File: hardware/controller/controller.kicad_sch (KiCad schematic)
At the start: 0 parts

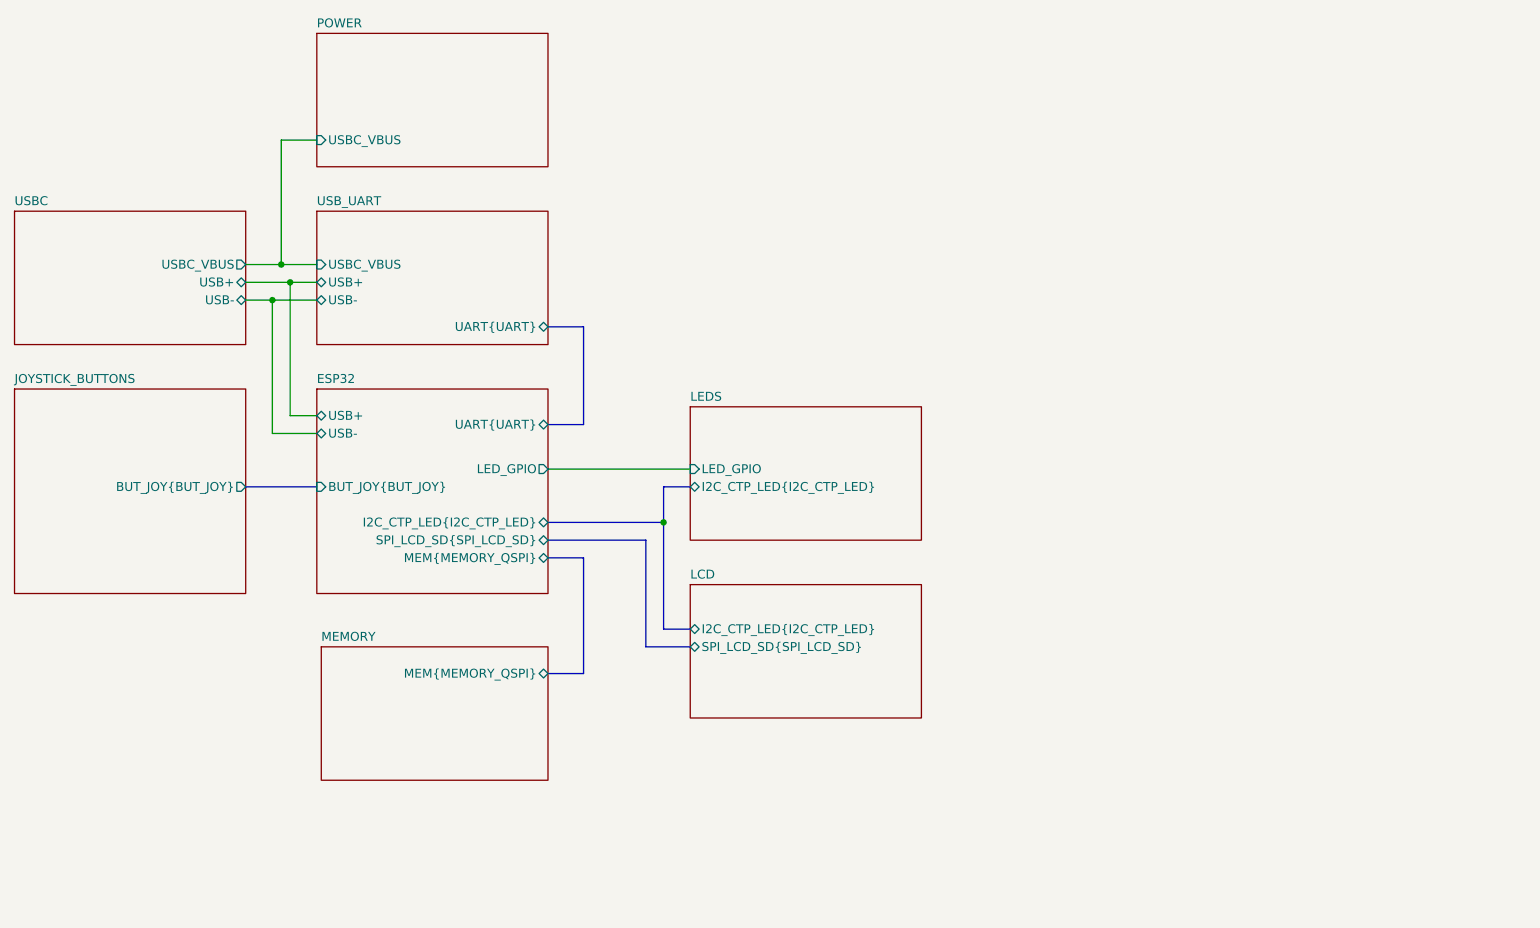
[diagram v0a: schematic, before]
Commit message: Moved LEDs around. Replaced some discrete resistors with resistor arrays. Added mounting holes. Added. Added a lot of actual components for passive elements
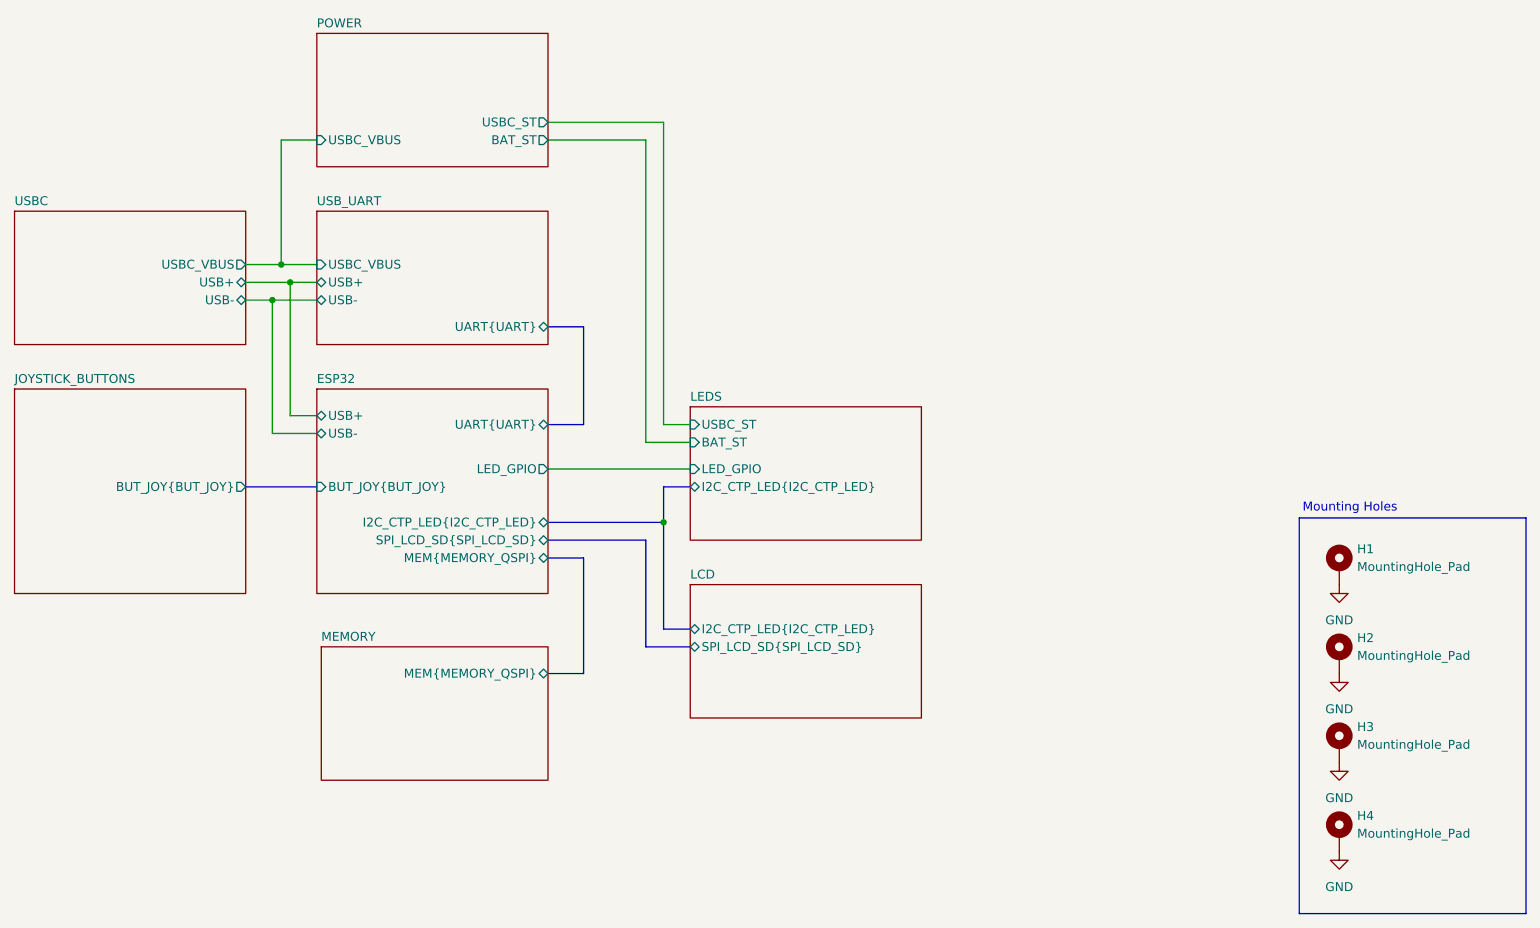
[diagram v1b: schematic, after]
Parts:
- added H1, H2, H3, H4: MountingHole_Pad, SamacSys_Parts:MountingHole_4.3mm_M4_ISO14580_Pad, symbol Mechanical:MountingHole_Pad
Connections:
- new net GND: H1.1, H2.1, H3.1, H4.1
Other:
- sheet LEDS ports: added BAT_ST, USBC_ST; removed none
- sheet POWER ports: added BAT_ST, USBC_ST; removed none
- note added: "Mounting Holes"
- title: Controller -> Remote Controller

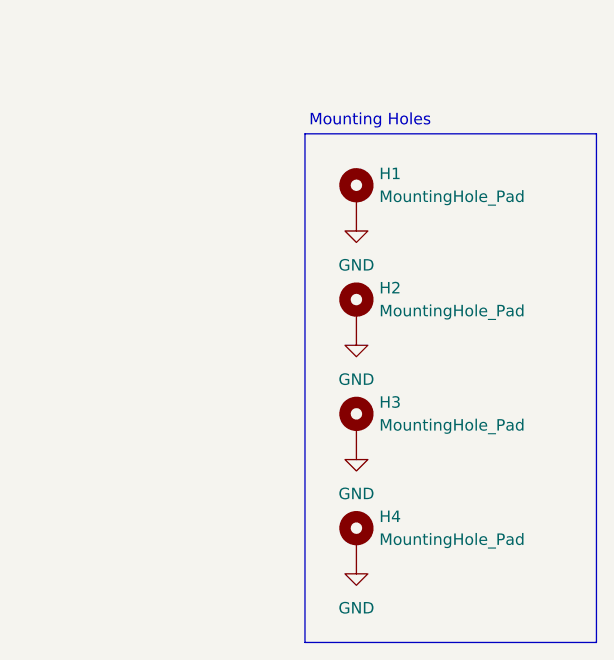
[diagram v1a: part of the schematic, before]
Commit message: ERC good to go. grouped all components on pcb
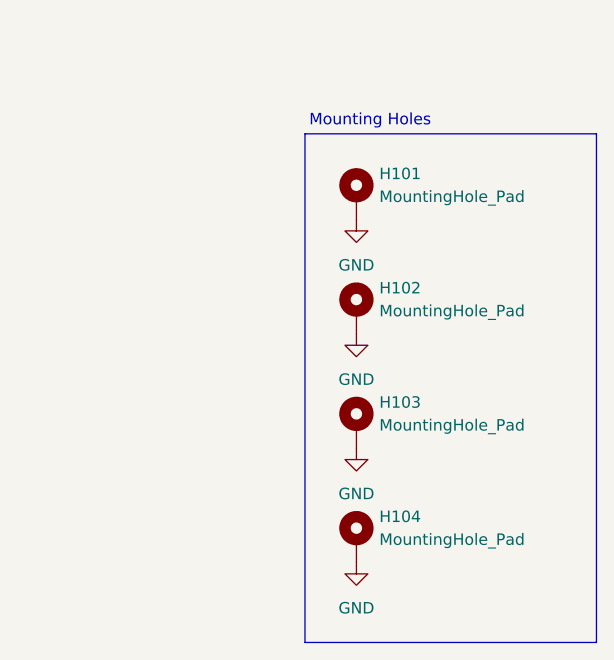
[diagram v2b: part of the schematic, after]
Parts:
- renumbered H1 to H101, H2 to H102, H3 to H103, H4 to H104
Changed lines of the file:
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@@
 		(dnp no)
 		(fields_autoplaced yes)
-		(property "Reference" "#PWR083"
+		(property "Reference" "#PWR0104"
 			(at 247.65 158.75 0)
 			(effects
@@
 			(project "controller"
 				(path "/869bea87-c885-4ead-826b-3f34ceacafad"
-					(reference "#PWR083")
+					(reference "#PWR0104")
 					(unit 1)
 				)
@@
 		(dnp no)
 		(fields_autoplaced yes)
-		(property "Reference" "H3"
+		(property "Reference" "H103"
 			(at 250.19 134.6199 0)
 			(effects
@@
 			(project "controller"
 				(path "/869bea87-c885-4ead-826b-3f34ceacafad"
-					(reference "H3")
+					(reference "H103")
 					(unit 1)
 				)
@@
 		(dnp no)
 		(fields_autoplaced yes)
-		(property "Reference" "#PWR082"
+		(property "Reference" "#PWR0103"
 			(at 247.65 146.05 0)
 			(effects
@@
 			(project "controller"
 				(path "/869bea87-c885-4ead-826b-3f34ceacafad"
-					(reference "#PWR082")
+					(reference "#PWR0103")
 					(unit 1)
 				)
@@
 		(dnp no)
 		(fields_autoplaced yes)
-		(property "Reference" "#PWR079"
+		(property "Reference" "#PWR0102"
 			(at 247.65 133.35 0)
 			(effects
@@
 			(project "controller"
 				(path "/869bea87-c885-4ead-826b-3f34ceacafad"
-					(reference "#PWR079")
+					(reference "#PWR0102")
 					(unit 1)
 				)
@@
 		(dnp no)
 		(fields_autoplaced yes)
-		(property "Reference" "#PWR021"
+		(property "Reference" "#PWR0101"
 			(at 247.65 120.65 0)
 			(effects
@@
 			(project ""
 				(path "/869bea87-c885-4ead-826b-3f34ceacafad"
-					(reference "#PWR021")
+					(reference "#PWR0101")
 					(unit 1)
 				)
@@
 		(dnp no)
 		(fields_autoplaced yes)
-		(property "Reference" "H4"
+		(property "Reference" "H104"
 			(at 250.19 147.3199 0)
 			(effects
@@
 			(project "controller"
 				(path "/869bea87-c885-4ead-826b-3f34ceacafad"
-					(reference "H4")
+					(reference "H104")
 					(unit 1)
 				)
@@
 		(dnp no)
 		(fields_autoplaced yes)
-		(property "Reference" "H1"
+		(property "Reference" "H101"
 			(at 250.19 109.2199 0)
 			(effects
@@
 			(project ""
 				(path "/869bea87-c885-4ead-826b-3f34ceacafad"
-					(reference "H1")
+					(reference "H101")
 					(unit 1)
 				)
@@
 		(dnp no)
 		(fields_autoplaced yes)
-		(property "Reference" "H2"
+		(property "Reference" "H102"
 			(at 250.19 121.9199 0)
 			(effects
@@
 			(project "controller"
 				(path "/869bea87-c885-4ead-826b-3f34ceacafad"
-					(reference "H2")
-					(unit 1)
-				)
+					(reference "H102")
+					(unit 1)
+				)

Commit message: a
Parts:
- added H105: MountingHole, MountingHole:MountingHole_2.2mm_M2_DIN965, symbol Mechanical:MountingHole
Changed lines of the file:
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@@
 	(text "Mounting Holes"
 		(exclude_from_sim no)
-		(at 249.174 103.378 0)
+		(at 248.412 86.614 0)
 		(effects
 			(font
@@
 	(text_box "\n"
 		(exclude_from_sim no)
-		(at 241.935 104.775 0)
-		(size 32.385 56.515)
+		(at 241.935 92.075 0)
+		(size 32.385 69.215)
 		(margins 0.9525 0.9525 0.9525 0.9525)
 		(stroke
@@
 	)
 	(symbol
+		(lib_id "Mechanical:MountingHole")
+		(at 247.65 100.33 0)
+		(unit 1)
+		(exclude_from_sim no)
+		(in_bom no)
+		(on_board yes)
+		(dnp no)
+		(fields_autoplaced yes)
+		(property "Reference" "H105"
+			(at 250.19 99.0599 0)
+			(effects
+				(font
+					(size 1.27 1.27)
+				)
+				(justify left)
+			)
+		)
+		(property "Value" "MountingHole"
+			(at 250.19 101.5999 0)
+			(effects
+				(font
+					(size 1.27 1.27)
+				)
+				(justify left)
+			)
+		)
+		(property "Footprint" "MountingHole:MountingHole_2.2mm_M2_DIN965"
+			(at 247.65 100.33 0)
+			(effects
+				(font
+					(size 1.27 1.27)
+				)
+				(hide yes)
+			)
+		)
+		(property "Datasheet" "~"
+			(at 247.65 100.33 0)
+			(effects
+				(font
+					(size 1.27 1.27)
+				)
+				(hide yes)
+			)
+		)
+		(property "Description" "Mounting Hole without connection"
+			(at 247.65 100.33 0)
+			(effects
+				(font
+					(size 1.27 1.27)
+				)
+				(hide yes)
+			)
+		)
+		(instances
+			(project ""
+				(path "/869bea87-c885-4ead-826b-3f34ceacafad"
+					(reference "H105")
+					(unit 1)
+				)
+			)
+		)
+	)
+	(symbol
 		(lib_id "Mechanical:MountingHole_Pad")
 		(at 247.65 124.46 0)
@@
 		(size 33.02 19.05)
 		(exclude_from_sim no)
-		(in_bom yes)
-		(on_board yes)
-		(dnp no)
-		(fields_autoplaced yes)
-		(stroke
+		(in_bom no)
+		(on_board no)
+		(dnp yes)
+		(fields_autoplaced yes)
+		(stroke

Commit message: save before nuke
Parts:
- renumbered H105 to H101, H101 to H102, H102 to H103, H103 to H104, H104 to H105
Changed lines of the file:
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@@
 		(dnp no)
 		(fields_autoplaced yes)
-		(property "Reference" "H103"
+		(property "Reference" "H104"
 			(at 250.19 134.6199 0)
 			(effects
@@
 			(project "controller"
 				(path "/869bea87-c885-4ead-826b-3f34ceacafad"
-					(reference "H103")
+					(reference "H104")
 					(unit 1)
 				)
@@
 		(dnp no)
 		(fields_autoplaced yes)
-		(property "Reference" "H104"
+		(property "Reference" "H105"
 			(at 250.19 147.3199 0)
 			(effects
@@
 			(project "controller"
 				(path "/869bea87-c885-4ead-826b-3f34ceacafad"
-					(reference "H104")
+					(reference "H105")
 					(unit 1)
 				)
@@
 		(dnp no)
 		(fields_autoplaced yes)
-		(property "Reference" "H101"
+		(property "Reference" "H102"
 			(at 250.19 109.2199 0)
 			(effects
@@
 			(project ""
 				(path "/869bea87-c885-4ead-826b-3f34ceacafad"
-					(reference "H101")
+					(reference "H102")
 					(unit 1)
 				)
@@
 		(dnp no)
 		(fields_autoplaced yes)
-		(property "Reference" "H105"
+		(property "Reference" "H101"
 			(at 250.19 99.0599 0)
 			(effects
@@
 			(project ""
 				(path "/869bea87-c885-4ead-826b-3f34ceacafad"
-					(reference "H105")
+					(reference "H101")
 					(unit 1)
 				)
@@
 		(dnp no)
 		(fields_autoplaced yes)
-		(property "Reference" "H102"
+		(property "Reference" "H103"
 			(at 250.19 121.9199 0)
 			(effects
@@
 			(project "controller"
 				(path "/869bea87-c885-4ead-826b-3f34ceacafad"
-					(reference "H102")
-					(unit 1)
-				)
+					(reference "H103")
+					(unit 1)
+				)
